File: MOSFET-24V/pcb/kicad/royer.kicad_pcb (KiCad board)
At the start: 2 copper layers, 40.6 x 59.7 mm, 26 parts, among them J1 Screw_Terminal_1x04, Q1 IRFB4410, Q2 IRFD110, Q3 IRFD110, Q4 IRFB4410

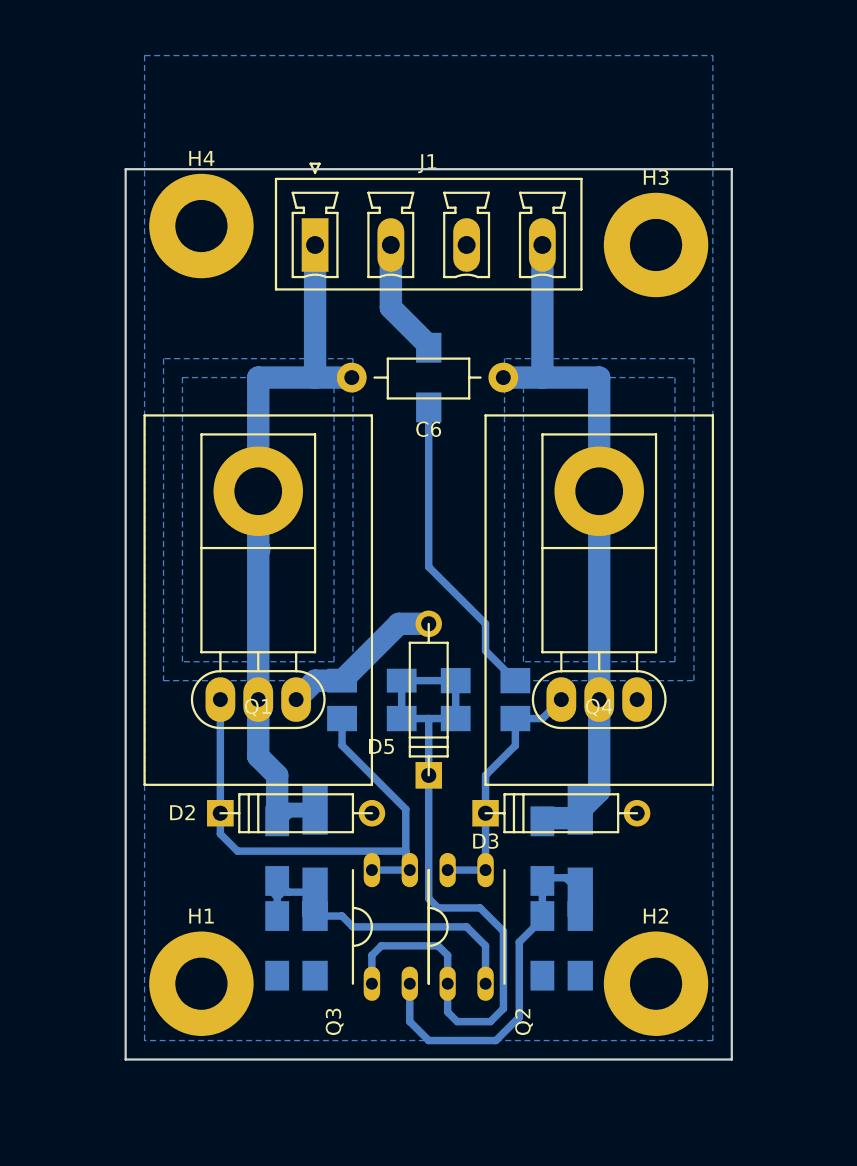
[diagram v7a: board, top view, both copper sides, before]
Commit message: increasing drill hole sizes in to-220 and screw terminal footprints
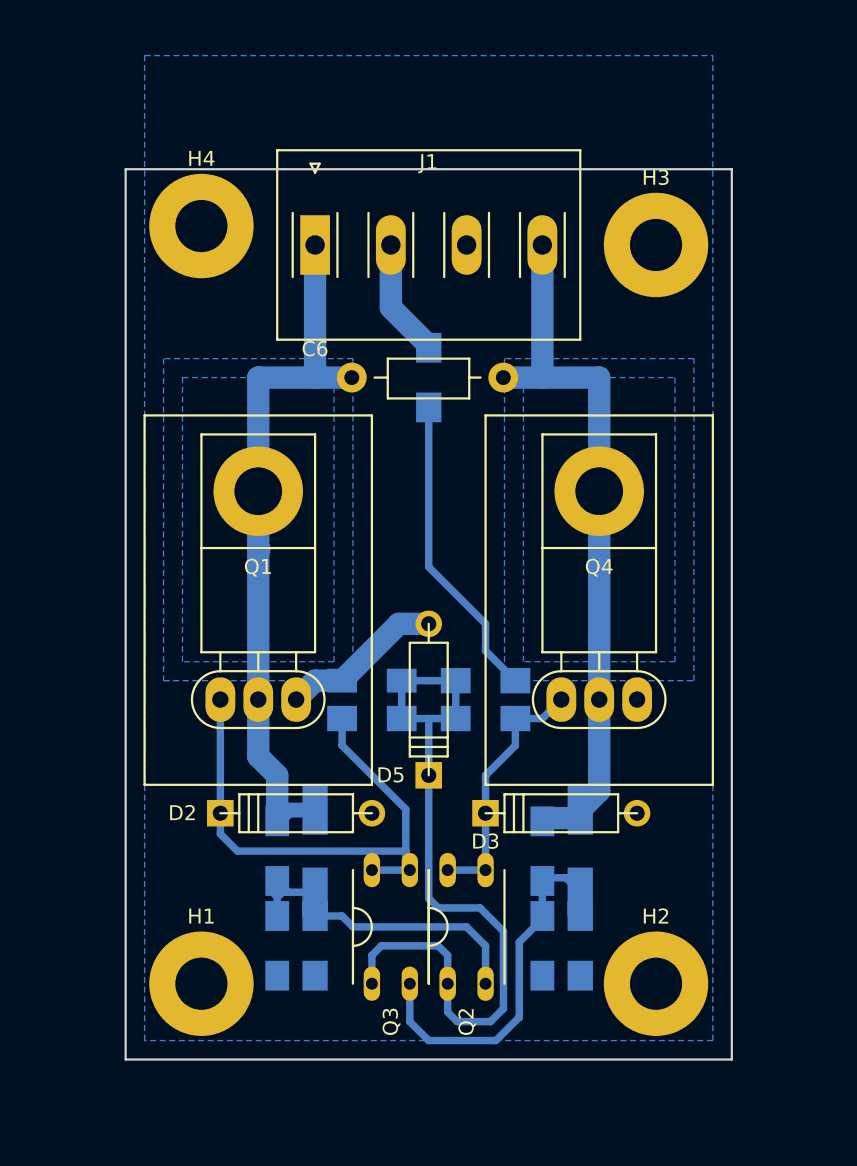
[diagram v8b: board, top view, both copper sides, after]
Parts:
- J1: footprint Connectors_Phoenix:PhoenixContact_MCV-G_04x5.08mm_Vertical -> screw-4-pin:screw-terminal-4-pin
